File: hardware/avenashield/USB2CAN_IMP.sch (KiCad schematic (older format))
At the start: 29 parts, among them U10 TXS0102DCT, U6 STM32F042C6Tx, U7 MCP2551-I-SN, Y3 16 MHz

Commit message: Added MiniPCIe latch clip and replaced onboard LEDs with connector
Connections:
- net +5V renamed BOARD_5V
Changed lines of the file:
@@
 $Descr A4 11693 8268
 encoding utf-8
-Sheet 5 7
+Sheet 3 7
 Title "USB2CAN for AvenaShield"
 Date ""
@@
 	1    0    0    -1
 $EndComp
-$Comp
-L power:+5V #PWR?
-U 1 1 5E4CF1CE
-P 7400 3450
-AR Path="/5E564EEA/5E4CF1CE" Ref="#PWR?"  Part="1"
-AR Path="/5E45C906/5E4CF1CE" Ref="#PWR0170"  Part="1"
-F 0 "#PWR0170" H 7400 3300 50  0001 C CNN
-F 1 "+5V" H 7415 3623 50  0000 C CNN
-F 2 "" H 7400 3450 50  0001 C CNN
-F 3 "" H 7400 3450 50  0001 C CNN
-	1    7400 3450
-	1    0    0    -1
-$EndComp
-Wire Wire Line
-	7400 3450 7400 3550
 $Comp
 L power:GNDREF #PWR?
@@
 	1    0    0    -1
 $EndComp
-$Comp
-L power:+5V #PWR?
-U 1 1 5E4CF1E2
-P 10200 900
-AR Path="/5E564EEA/5E4CF1E2" Ref="#PWR?"  Part="1"
-AR Path="/5E45C906/5E4CF1E2" Ref="#PWR0179"  Part="1"
-F 0 "#PWR0179" H 10200 750 50  0001 C CNN
-F 1 "+5V" H 10215 1073 50  0000 C CNN
-F 2 "" H 10200 900 50  0001 C CNN
-F 3 "" H 10200 900 50  0001 C CNN
-	1    10200 900
-	1    0    0    -1
-$EndComp
 Text HLabel 9650 1100 0    50   Input ~ 0
 BOARD_3v3
-Text HLabel 9650 1250 0    50   Input ~ 0
+Text HLabel 7200 3250 0    50   Input ~ 0
 BOARD_5V
 Wire Wire Line
@@
 Wire Wire Line
 	9900 1100 9900 900
-Wire Wire Line
-	10200 900  10200 1250
-Wire Wire Line
-	10200 1250 9650 1250
 Text HLabel 9650 1450 0    50   Input ~ 0
 BOARD_GND
@@
 $EndComp
 $Comp
-L power:+5V #PWR0189
-U 1 1 5E5B678E
-P 5700 4700
-F 0 "#PWR0189" H 5700 4550 50  0001 C CNN
-F 1 "+5V" H 5715 4873 50  0000 C CNN
-F 2 "" H 5700 4700 50  0001 C CNN
-F 3 "" H 5700 4700 50  0001 C CNN
-	1    5700 4700
-	1    0    0    -1
-$EndComp
-$Comp
 L power:GNDREF #PWR?
 U 1 1 5E5C33C4
@@
 Wire Wire Line
 	5500 4700 5500 4750
-Wire Wire Line
-	5700 4700 5700 4750
 $Comp
 L Device:C C53
@@
 Wire Wire Line
 	4950 5950 5200 5950
+Wire Wire Line
+	5700 3550 7400 3550
+Wire Wire Line
+	5700 3550 5700 4750
+Wire Wire Line
+	7200 3250 7400 3250
+Wire Wire Line
+	7400 3250 7400 3550
 $EndSCHEMATC

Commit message: Changed footprints for CAN connectors and replaced 3D models for headers
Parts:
- C39, C40, C41, C42, C43, C44, C45, C46, C47, C48, C49, C50, C51, C52, C53, C54: footprint Capacitor_SMD:C_0603_1608Metric -> Capacitor_SMD:C_0805_2012Metric_Pad1.15x1.40mm_HandSolder
- R17, R18, R19, R20, R25: footprint Resistor_SMD:R_1206_3216Metric -> Resistor_SMD:R_0805_2012Metric_Pad1.15x1.40mm_HandSolder
- Y3: footprint Crystal:Crystal_SMD_2016-4Pin_2.0x1.6mm -> Crystal:Crystal_SMD_HC49-SD
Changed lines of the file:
@@
 F 0 "C41" H 6165 1096 50  0000 L CNN
 F 1 "0.1u" H 6165 1005 50  0000 L CNN
-F 2 "Capacitor_SMD:C_0603_1608Metric" H 6088 900 50  0001 C CNN
+F 2 "Capacitor_SMD:C_0805_2012Metric_Pad1.15x1.40mm_HandSolder" H 6088 900 50  0001 C CNN
 F 3 "~" H 6050 1050 50  0001 C CNN
 	1    6050 1050
@@
 F 0 "C42" H 5265 1996 50  0000 L CNN
 F 1 "0.1u" H 5265 1905 50  0000 L CNN
-F 2 "Capacitor_SMD:C_0603_1608Metric" H 5188 1800 50  0001 C CNN
+F 2 "Capacitor_SMD:C_0805_2012Metric_Pad1.15x1.40mm_HandSolder" H 5188 1800 50  0001 C CNN
 F 3 "~" H 5150 1950 50  0001 C CNN
 	1    5150 1950
@@
 F 0 "C43" H 5615 1996 50  0000 L CNN
 F 1 "0.1u" H 5615 1905 50  0000 L CNN
-F 2 "Capacitor_SMD:C_0603_1608Metric" H 5538 1800 50  0001 C CNN
+F 2 "Capacitor_SMD:C_0805_2012Metric_Pad1.15x1.40mm_HandSolder" H 5538 1800 50  0001 C CNN
 F 3 "~" H 5500 1950 50  0001 C CNN
 	1    5500 1950
@@
 F 0 "C44" H 5965 1996 50  0000 L CNN
 F 1 "4.7u" H 5965 1905 50  0000 L CNN
-F 2 "Capacitor_SMD:C_0603_1608Metric" H 5888 1800 50  0001 C CNN
+F 2 "Capacitor_SMD:C_0805_2012Metric_Pad1.15x1.40mm_HandSolder" H 5888 1800 50  0001 C CNN
 F 3 "~" H 5850 1950 50  0001 C CNN
 	1    5850 1950
@@
 F 0 "C45" H 6415 1996 50  0000 L CNN
 F 1 "0.1u" H 6415 1905 50  0000 L CNN
-F 2 "Capacitor_SMD:C_0603_1608Metric" H 6338 1800 50  0001 C CNN
+F 2 "Capacitor_SMD:C_0805_2012Metric_Pad1.15x1.40mm_HandSolder" H 6338 1800 50  0001 C CNN
 F 3 "~" H 6300 1950 50  0001 C CNN
 	1    6300 1950
@@
 F 0 "C46" H 6765 1996 50  0000 L CNN
 F 1 "0.1u" H 6765 1905 50  0000 L CNN
-F 2 "Capacitor_SMD:C_0603_1608Metric" H 6688 1800 50  0001 C CNN
+F 2 "Capacitor_SMD:C_0805_2012Metric_Pad1.15x1.40mm_HandSolder" H 6688 1800 50  0001 C CNN
 F 3 "~" H 6650 1950 50  0001 C CNN
 	1    6650 1950
@@
 F 0 "C47" H 7115 1996 50  0000 L CNN
 F 1 "4.7u" H 7115 1905 50  0000 L CNN
-F 2 "Capacitor_SMD:C_0603_1608Metric" H 7038 1800 50  0001 C CNN
+F 2 "Capacitor_SMD:C_0805_2012Metric_Pad1.15x1.40mm_HandSolder" H 7038 1800 50  0001 C CNN
 F 3 "~" H 7000 1950 50  0001 C CNN
 	1    7000 1950
@@
 F 0 "C48" H 7565 1996 50  0000 L CNN
 F 1 "10n" H 7565 1905 50  0000 L CNN
-F 2 "Capacitor_SMD:C_0603_1608Metric" H 7488 1800 50  0001 C CNN
+F 2 "Capacitor_SMD:C_0805_2012Metric_Pad1.15x1.40mm_HandSolder" H 7488 1800 50  0001 C CNN
 F 3 "~" H 7450 1950 50  0001 C CNN
 	1    7450 1950
@@
 F 0 "C49" H 7915 1996 50  0000 L CNN
 F 1 "1u" H 7915 1905 50  0000 L CNN
-F 2 "Capacitor_SMD:C_0603_1608Metric" H 7838 1800 50  0001 C CNN
+F 2 "Capacitor_SMD:C_0805_2012Metric_Pad1.15x1.40mm_HandSolder" H 7838 1800 50  0001 C CNN
 F 3 "~" H 7800 1950 50  0001 C CNN
 	1    7800 1950
@@
 F 0 "C50" H 8315 1996 50  0000 L CNN
 F 1 "0.1u" H 8315 1905 50  0000 L CNN
-F 2 "Capacitor_SMD:C_0603_1608Metric" H 8238 1800 50  0001 C CNN
+F 2 "Capacitor_SMD:C_0805_2012Metric_Pad1.15x1.40mm_HandSolder" H 8238 1800 50  0001 C CNN
 F 3 "~" H 8200 1950 50  0001 C CNN
 	1    8200 1950
@@
 F 0 "C51" H 8665 1996 50  0000 L CNN
 F 1 "4.7u" H 8665 1905 50  0000 L CNN
-F 2 "Capacitor_SMD:C_0603_1608Metric" H 8588 1800 50  0001 C CNN
+F 2 "Capacitor_SMD:C_0805_2012Metric_Pad1.15x1.40mm_HandSolder" H 8588 1800 50  0001 C CNN
 F 3 "~" H 8550 1950 50  0001 C CNN
 	1    8550 1950
@@
 F 0 "C54" V 7498 3550 50  0000 C CNN
 F 1 "0.1u" V 7589 3550 50  0000 C CNN
-F 2 "Capacitor_SMD:C_0603_1608Metric" H 7788 3400 50  0001 C CNN
+F 2 "Capacitor_SMD:C_0805_2012Metric_Pad1.15x1.40mm_HandSolder" H 7788 3400 50  0001 C CNN
 F 3 "~" H 7750 3550 50  0001 C CNN
 	1    7750 3550
@@
 F 0 "R19" H 3268 2896 50  0000 L CNN
 F 1 "510" H 3268 2805 50  0000 L CNN
-F 2 "Resistor_SMD:R_1206_3216Metric" V 3240 2840 50  0001 C CNN
+F 2 "Resistor_SMD:R_0805_2012Metric_Pad1.15x1.40mm_HandSolder" V 3240 2840 50  0001 C CNN
 F 3 "~" H 3200 2850 50  0001 C CNN
 	1    3200 2850
@@
 F 0 "C40" H 2065 2946 50  0000 L CNN
 F 1 "18p" H 2065 2855 50  0000 L CNN
-F 2 "Capacitor_SMD:C_0603_1608Metric" H 1988 2750 50  0001 C CNN
+F 2 "Capacitor_SMD:C_0805_2012Metric_Pad1.15x1.40mm_HandSolder" H 1988 2750 50  0001 C CNN
 F 3 "~" H 1950 2900 50  0001 C CNN
 	1    1950 2900
@@
 F 0 "Y3" H 1650 2818 50  0000 C CNN
 F 1 "16 MHz" H 1650 2727 50  0000 C CNN
-F 2 "Crystal:Crystal_SMD_2016-4Pin_2.0x1.6mm" H 1650 2550 50  0001 C CNN
+F 2 "Crystal:Crystal_SMD_HC49-SD" H 1650 2550 50  0001 C CNN
 F 3 "~" H 1650 2550 50  0001 C CNN
 	1    1650 2550
@@
 F 0 "C39" H 1465 2946 50  0000 L CNN
 F 1 "18p" H 1465 2855 50  0000 L CNN
-F 2 "Capacitor_SMD:C_0603_1608Metric" H 1388 2750 50  0001 C CNN
+F 2 "Capacitor_SMD:C_0805_2012Metric_Pad1.15x1.40mm_HandSolder" H 1388 2750 50  0001 C CNN
 F 3 "~" H 1350 2900 50  0001 C CNN
 	1    1350 2900
@@
 F 0 "R17" H 2168 4196 50  0000 L CNN
 F 1 "120" H 2168 4105 50  0000 L CNN
-F 2 "Resistor_SMD:R_1206_3216Metric" V 2140 4140 50  0001 C CNN
+F 2 "Resistor_SMD:R_0805_2012Metric_Pad1.15x1.40mm_HandSolder" V 2140 4140 50  0001 C CNN
 F 3 "~" H 2100 4150 50  0001 C CNN
 	1    2100 4150
@@
 F 0 "R18" H 2518 4196 50  0000 L CNN
 F 1 "120" H 2518 4105 50  0000 L CNN
-F 2 "Resistor_SMD:R_1206_3216Metric" V 2490 4140 50  0001 C CNN
+F 2 "Resistor_SMD:R_0805_2012Metric_Pad1.15x1.40mm_HandSolder" V 2490 4140 50  0001 C CNN
 F 3 "~" H 2450 4150 50  0001 C CNN
 	1    2450 4150
@@
 F 0 "R20" H 8818 4296 50  0000 L CNN
 F 1 "120" H 8818 4205 50  0000 L CNN
-F 2 "Resistor_SMD:R_1206_3216Metric" V 8790 4240 50  0001 C CNN
+F 2 "Resistor_SMD:R_0805_2012Metric_Pad1.15x1.40mm_HandSolder" V 8790 4240 50  0001 C CNN
 F 3 "~" H 8750 4250 50  0001 C CNN
 	1    8750 4250
@@
 F 0 "C53" H 6015 4996 50  0000 L CNN
 F 1 "0.1u" H 6015 4905 50  0000 L CNN
-F 2 "Capacitor_SMD:C_0603_1608Metric" H 5938 4800 50  0001 C CNN
+F 2 "Capacitor_SMD:C_0805_2012Metric_Pad1.15x1.40mm_HandSolder" H 5938 4800 50  0001 C CNN
 F 3 "~" H 5900 4950 50  0001 C CNN
 	1    5900 4950
@@
 F 0 "C52" H 5350 5050 50  0000 L CNN
 F 1 "0.1u" H 5300 4850 50  0000 L CNN
-F 2 "Capacitor_SMD:C_0603_1608Metric" H 5288 4800 50  0001 C CNN
+F 2 "Capacitor_SMD:C_0805_2012Metric_Pad1.15x1.40mm_HandSolder" H 5288 4800 50  0001 C CNN
 F 3 "~" H 5250 4950 50  0001 C CNN
 	1    5250 4950
@@
 F 0 "R25" H 4718 6296 50  0000 L CNN
 F 1 "10k" H 4718 6205 50  0000 L CNN
-F 2 "Resistor_SMD:R_1206_3216Metric" V 4690 6240 50  0001 C CNN
+F 2 "Resistor_SMD:R_0805_2012Metric_Pad1.15x1.40mm_HandSolder" V 4690 6240 50  0001 C CNN
 F 3 "~" H 4650 6250 50  0001 C CNN
 	1    4650 6250

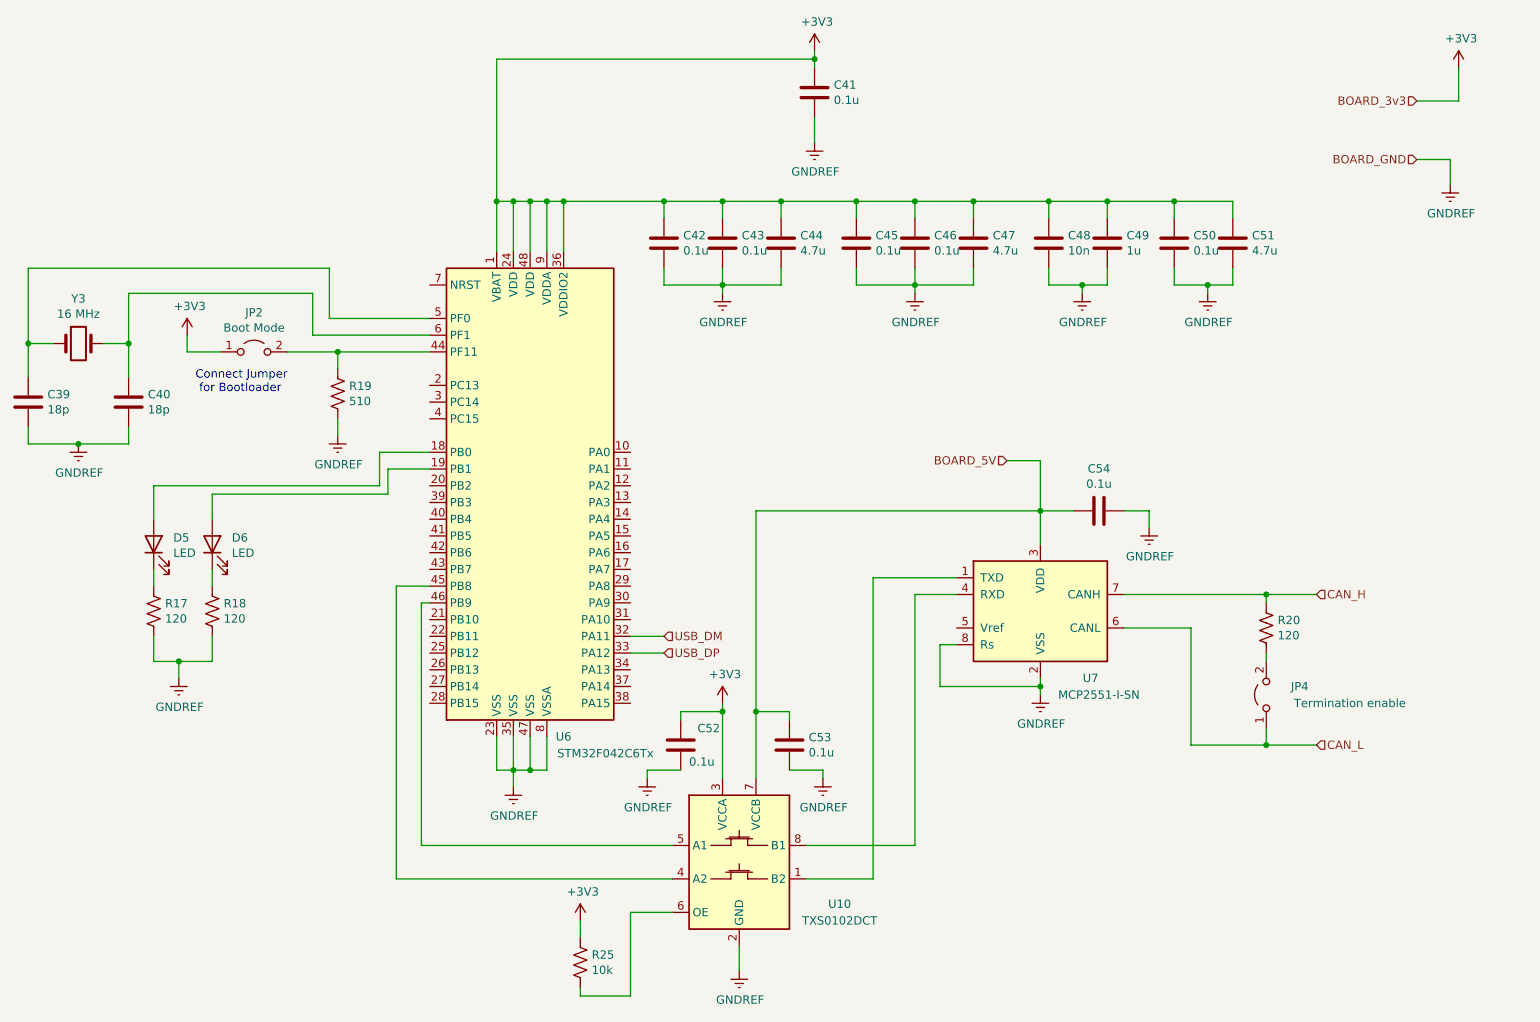
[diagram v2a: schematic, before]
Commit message: Improved I2C bus routing
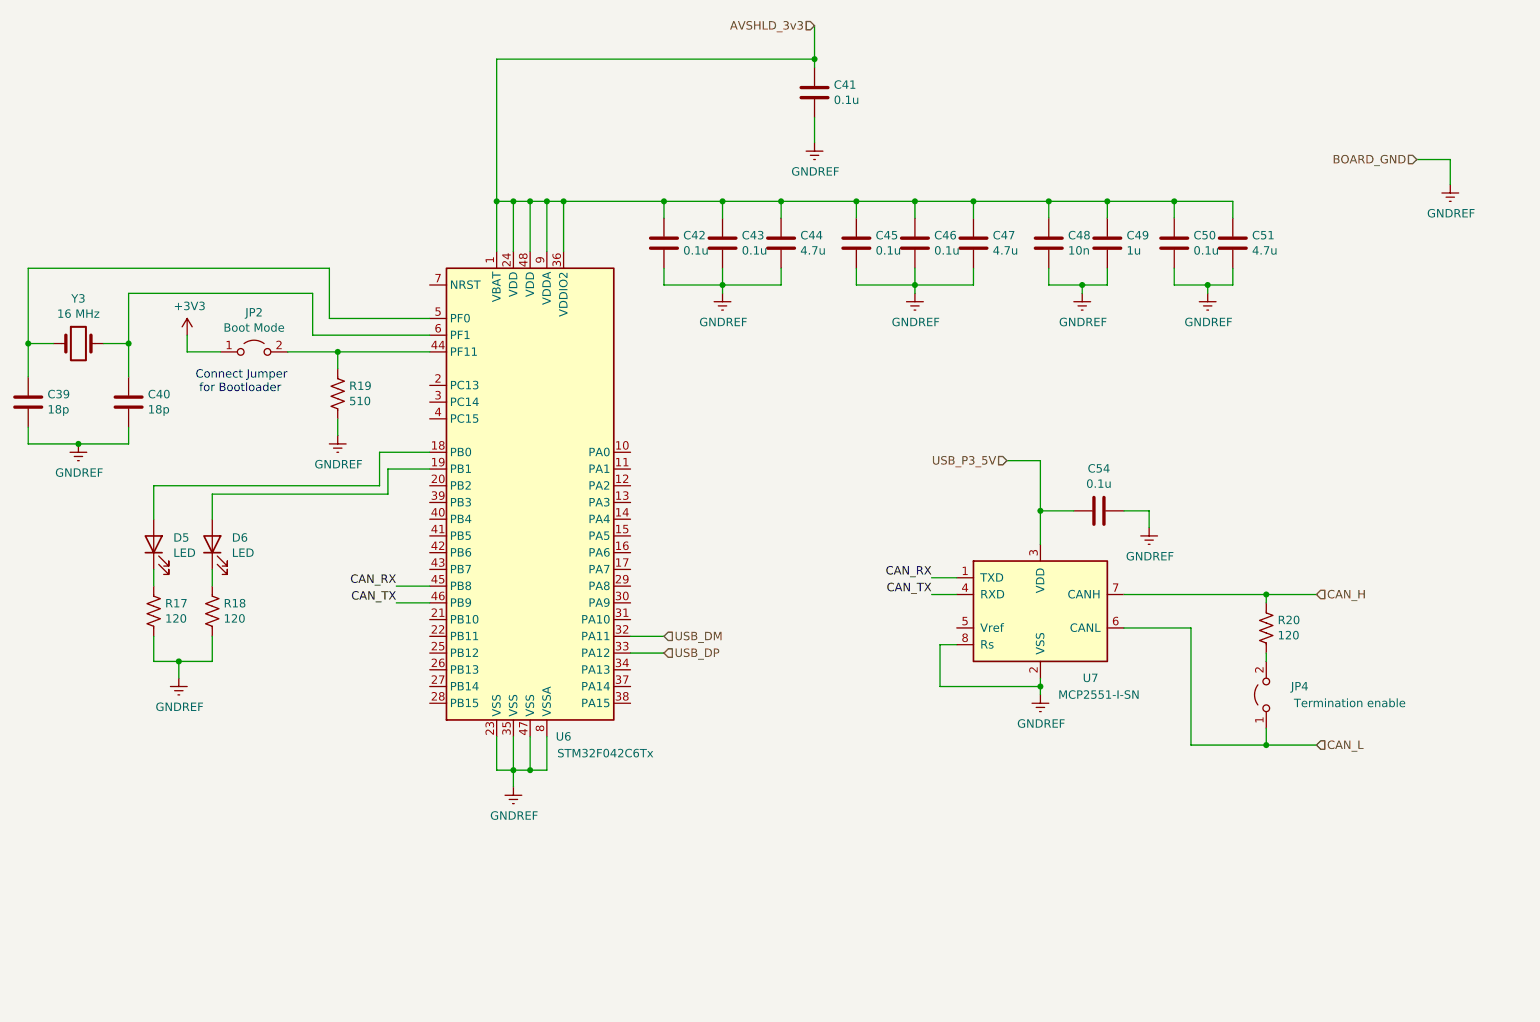
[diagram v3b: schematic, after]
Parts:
- removed C52, C53: 0.1u, Capacitor_SMD:C_0805_2012Metric_Pad1.15x1.40mm_HandSolder, symbol Device:C
- removed R25: 10k, Resistor_SMD:R_0805_2012Metric_Pad1.15x1.40mm_HandSolder, symbol Device:R_US
- removed U10: TXS0102DCT, Package_SO:SSOP-8_2.95x2.8mm_P0.65mm, symbol Logic_LevelTranslator:TXS0102DCT
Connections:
- net +3V3: no longer C41.1, C42.1, C43.1, C44.1, C45.1, C46.1, C47.1, C48.1, C49.1, C50.1, C51.1, U6.1 (VBAT), U6.24 (VDD), U6.36 (VDDIO2), U6.48 (VDD), U6.9 (VDDA)
- net CAN_RX: now reaches U7.1 (TXD)
- net CAN_RX: now also U6.45 (PB8)
- net CAN_TX: now reaches U7.4 (RXD)
- net CAN_TX: now also U6.46 (PB9)
- net BOARD_5V renamed USB_P3_5V
- new net AVSHLD_3v3: C41.1, C42.1, C43.1, C44.1, C45.1, C46.1, C47.1, C48.1, C49.1, C50.1, C51.1, U6.1 (VBAT), U6.24 (VDD), U6.36 (VDDIO2), U6.48 (VDD), U6.9 (VDDA)
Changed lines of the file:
@@
 $EndComp
-Wire Wire Line
-	6050 800  6050 850
 Wire Wire Line
 	6050 1200 6050 1350
@@
 Wire Wire Line
 	3750 4000 3550 4000
-Wire Wire Line
-	3750 4100 3700 4100
 $Comp
 L Jumper:Jumper_2_Open JP?
@@
 F 3 "" H 2300 2500 50  0001 C CNN
 	1    2300 2500
-	1    0    0    -1
-$EndComp
-$Comp
-L power:+3V3 #PWR?
-U 1 1 5E5B1DF1
-P 6050 800
-AR Path="/5E564EEA/5E5B1DF1" Ref="#PWR?"  Part="1"
-AR Path="/5E45C906/5E5B1DF1" Ref="#PWR0174"  Part="1"
-F 0 "#PWR0174" H 6050 650 50  0001 C CNN
-F 1 "+3V3" H 6065 973 50  0000 C CNN
-F 2 "" H 6050 800 50  0001 C CNN
-F 3 "" H 6050 800 50  0001 C CNN
-	1    6050 800
 	1    0    0    -1
 $EndComp
@@
 Wire Wire Line
 	7900 4250 8300 4250
-$Comp
-L power:+3V3 #PWR?
-U 1 1 5E4CF1E1
-P 9900 900
-AR Path="/5E564EEA/5E4CF1E1" Ref="#PWR?"  Part="1"
-AR Path="/5E45C906/5E4CF1E1" Ref="#PWR0178"  Part="1"
-F 0 "#PWR0178" H 9900 750 50  0001 C CNN
-F 1 "+3V3" H 9915 1073 50  0000 C CNN
-F 2 "" H 9900 900 50  0001 C CNN
-F 3 "" H 9900 900 50  0001 C CNN
-	1    9900 900
-	1    0    0    -1
-$EndComp
-Text HLabel 9650 1100 0    50   Input ~ 0
-BOARD_3v3
 Text HLabel 7200 3250 0    50   Input ~ 0
-BOARD_5V
-Wire Wire Line
-	9650 1100 9900 1100
-Wire Wire Line
-	9900 1100 9900 900
+USB_P3_5V
 Text HLabel 9650 1450 0    50   Input ~ 0
 BOARD_GND
@@
 	9050 4950 8750 4950
 Connection ~ 8750 4950
-$Comp
-L Logic_LevelTranslator:TXS0102DCT U10
-U 1 1 5E59C762
-P 5600 5650
-F 0 "U10" H 6200 5400 50  0000 C CNN
-F 1 "TXS0102DCT" H 6200 5300 50  0000 C CNN
-F 2 "Package_SO:SSOP-8_2.95x2.8mm_P0.65mm" H 5600 5100 50  0001 C CNN
-F 3 "http://www.ti.com/lit/gpn/txs0102" H 5600 5630 50  0001 C CNN
-	1    5600 5650
-	1    0    0    -1
-$EndComp
-Wire Wire Line
-	3700 4100 3700 5550
-Wire Wire Line
-	3700 5550 5200 5550
-Wire Wire Line
-	3550 4000 3550 5750
-Wire Wire Line
-	3550 5750 5200 5750
-Wire Wire Line
-	6000 5750 6400 5750
-Wire Wire Line
-	6400 5750 6400 3950
-Wire Wire Line
-	6400 3950 6900 3950
-Wire Wire Line
-	6900 4050 6650 4050
-Wire Wire Line
-	6650 4050 6650 5550
-Wire Wire Line
-	6650 5550 6000 5550
-$Comp
-L power:+3V3 #PWR0188
-U 1 1 5E5B5FD0
-P 5500 4700
-F 0 "#PWR0188" H 5500 4550 50  0001 C CNN
-F 1 "+3V3" H 5515 4873 50  0000 C CNN
-F 2 "" H 5500 4700 50  0001 C CNN
-F 3 "" H 5500 4700 50  0001 C CNN
-	1    5500 4700
-	1    0    0    -1
-$EndComp
-$Comp
-L power:GNDREF #PWR?
-U 1 1 5E5C33C4
-P 5600 6300
-AR Path="/5E564EEA/5E5C33C4" Ref="#PWR?"  Part="1"
-AR Path="/5E45C906/5E5C33C4" Ref="#PWR0190"  Part="1"
-F 0 "#PWR0190" H 5600 6050 50  0001 C CNN
-F 1 "GNDREF" H 5605 6127 50  0000 C CNN
-F 2 "" H 5600 6300 50  0001 C CNN
-F 3 "" H 5600 6300 50  0001 C CNN
-	1    5600 6300
-	1    0    0    -1
-$EndComp
-Wire Wire Line
-	5600 6300 5600 6150
-Wire Wire Line
-	5500 4700 5500 4750
-$Comp
-L Device:C C53
-U 1 1 5E5DE230
-P 5900 4950
-F 0 "C53" H 6015 4996 50  0000 L CNN
-F 1 "0.1u" H 6015 4905 50  0000 L CNN
-F 2 "Capacitor_SMD:C_0805_2012Metric_Pad1.15x1.40mm_HandSolder" H 5938 4800 50  0001 C CNN
-F 3 "~" H 5900 4950 50  0001 C CNN
-	1    5900 4950
-	1    0    0    -1
-$EndComp
-$Comp
-L Device:C C52
-U 1 1 5E5DE56C
-P 5250 4950
-F 0 "C52" H 5350 5050 50  0000 L CNN
-F 1 "0.1u" H 5300 4850 50  0000 L CNN
-F 2 "Capacitor_SMD:C_0805_2012Metric_Pad1.15x1.40mm_HandSolder" H 5288 4800 50  0001 C CNN
-F 3 "~" H 5250 4950 50  0001 C CNN
-	1    5250 4950
-	1    0    0    -1
-$EndComp
-$Comp
-L power:GNDREF #PWR?
-U 1 1 5E5DF54C
-P 5050 5150
-AR Path="/5E564EEA/5E5DF54C" Ref="#PWR?"  Part="1"
-AR Path="/5E45C906/5E5DF54C" Ref="#PWR0191"  Part="1"
-F 0 "#PWR0191" H 5050 4900 50  0001 C CNN
-F 1 "GNDREF" H 5055 4977 50  0000 C CNN
-F 2 "" H 5050 5150 50  0001 C CNN
-F 3 "" H 5050 5150 50  0001 C CNN
-	1    5050 5150
-	1    0    0    -1
-$EndComp
-$Comp
-L power:GNDREF #PWR?
-U 1 1 5E5DFA9E
-P 6100 5150
-AR Path="/5E564EEA/5E5DFA9E" Ref="#PWR?"  Part="1"
-AR Path="/5E45C906/5E5DFA9E" Ref="#PWR0192"  Part="1"
-F 0 "#PWR0192" H 6100 4900 50  0001 C CNN
-F 1 "GNDREF" H 6105 4977 50  0000 C CNN
-F 2 "" H 6100 5150 50  0001 C CNN
-F 3 "" H 6100 5150 50  0001 C CNN
-	1    6100 5150
-	1    0    0    -1
-$EndComp
-Wire Wire Line
-	5050 5150 5050 5100
-Wire Wire Line
-	5050 5100 5250 5100
-Wire Wire Line
-	5900 5100 6100 5100
-Wire Wire Line
-	6100 5100 6100 5150
-Wire Wire Line
-	5250 4800 5250 4750
-Wire Wire Line
-	5250 4750 5500 4750
-Connection ~ 5500 4750
-Wire Wire Line
-	5500 4750 5500 5150
-Wire Wire Line
-	5700 4750 5900 4750
-Wire Wire Line
-	5900 4750 5900 4800
-Connection ~ 5700 4750
-Wire Wire Line
-	5700 4750 5700 5150
-$Comp
-L Device:R_US R25
-U 1 1 5E701AFE
-P 4650 6250
-F 0 "R25" H 4718 6296 50  0000 L CNN
-F 1 "10k" H 4718 6205 50  0000 L CNN
-F 2 "Resistor_SMD:R_0805_2012Metric_Pad1.15x1.40mm_HandSolder" V 4690 6240 50  0001 C CNN
-F 3 "~" H 4650 6250 50  0001 C CNN
-	1    4650 6250
-	1    0    0    -1
-$EndComp
-$Comp
-L power:+3V3 #PWR0193
-U 1 1 5E702345
-P 4650 6000
-F 0 "#PWR0193" H 4650 5850 50  0001 C CNN
-F 1 "+3V3" H 4665 6173 50  0000 C CNN
-F 2 "" H 4650 6000 50  0001 C CNN
-F 3 "" H 4650 6000 50  0001 C CNN
-	1    4650 6000
-	1    0    0    -1
-$EndComp
-Wire Wire Line
-	4650 6000 4650 6100
-Wire Wire Line
-	4650 6400 4650 6450
-Wire Wire Line
-	4650 6450 4950 6450
-Wire Wire Line
-	4950 6450 4950 5950
-Wire Wire Line
-	4950 5950 5200 5950
-Wire Wire Line
-	5700 3550 7400 3550
-Wire Wire Line
-	5700 3550 5700 4750
 Wire Wire Line
 	7200 3250 7400 3250
 Wire Wire Line
 	7400 3250 7400 3550
+Text HLabel 6050 650  0    50   Input ~ 0
+AVSHLD_3v3
+Wire Wire Line
+	6050 650  6050 850
+Wire Wire Line
+	3550 4100 3750 4100
+Text Label 3550 4000 2    50   ~ 0
+CAN_RX
+Text Label 3550 4100 2    50   ~ 0
+CAN_TX
+Text Label 6750 3950 2    50   ~ 0
+CAN_RX
+Text Label 6750 4050 2    50   ~ 0
+CAN_TX
+Wire Wire Line
+	6750 3950 6900 3950
+Wire Wire Line
+	6900 4050 6750 4050
 $EndSCHEMATC
